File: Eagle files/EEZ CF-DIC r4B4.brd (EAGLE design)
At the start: 155 x 90 mm, 236 parts, among them IC1 VIPer35L, IC2 SI8233BB-D-IS1, IC3 LM5041B, IC4 LM258D, IC5 IR11688STRPBF, IC6 TL072, IC7 TL103W, P1 T910W-50K, Q1 MMBT5551, Q2 C3M0280090D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

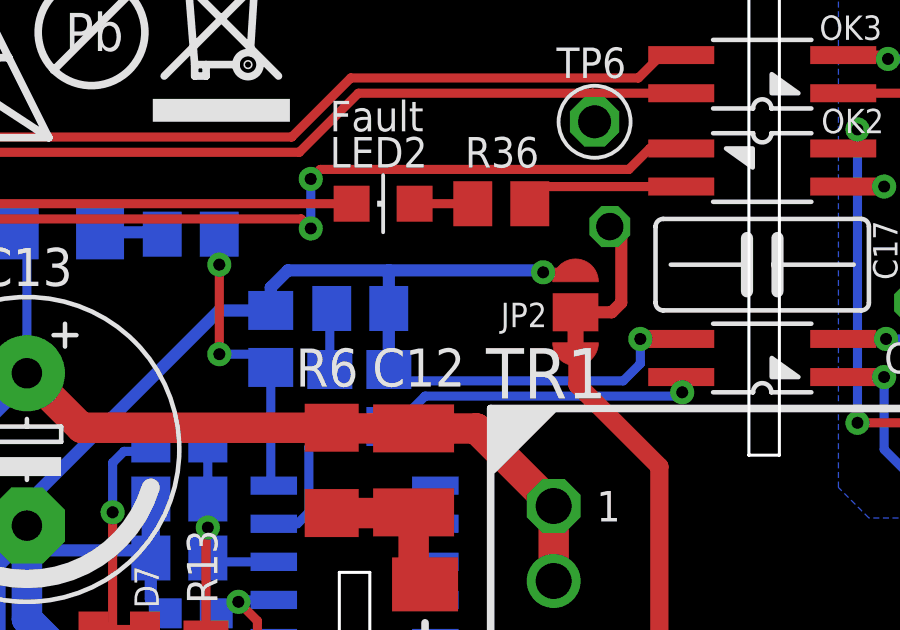
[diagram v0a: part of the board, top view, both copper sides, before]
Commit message: JP2 rotated
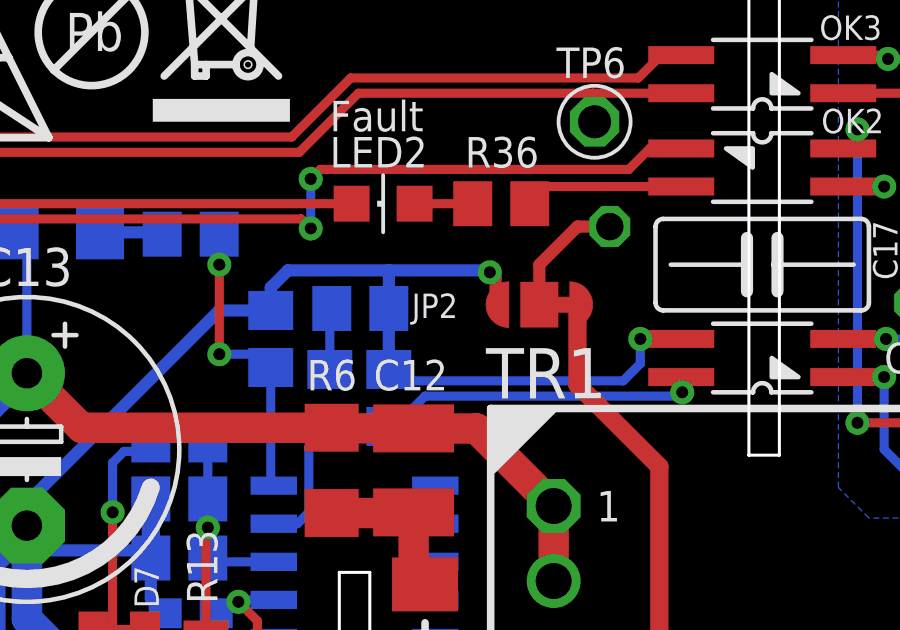
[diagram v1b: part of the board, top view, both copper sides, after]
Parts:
- moved JP2 1.23 mm to (99.0, 26.2), turned to 180 degrees
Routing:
- net 0V: track 763.4 -> 761.7 mm
- net PE: track 292.3 -> 293.8 mm
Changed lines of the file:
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@@
 <layer number="27" name="tValues" color="12" fill="1" visible="no" active="yes"/>
 <layer number="28" name="bValues" color="10" fill="1" visible="no" active="yes"/>
-<layer number="29" name="tStop" color="7" fill="1" visible="no" active="yes"/>
+<layer number="29" name="tStop" color="7" fill="1" visible="yes" active="yes"/>
 <layer number="30" name="bStop" color="7" fill="1" visible="no" active="yes"/>
 <layer number="31" name="tCream" color="7" fill="4" visible="no" active="yes"/>
@@
 <layer number="37" name="tTest" color="7" fill="1" visible="no" active="yes"/>
 <layer number="38" name="bTest" color="7" fill="1" visible="no" active="yes"/>
-<layer number="39" name="tKeepout" color="15" fill="1" visible="no" active="yes"/>
+<layer number="39" name="tKeepout" color="15" fill="1" visible="yes" active="yes"/>
 <layer number="40" name="bKeepout" color="5" fill="1" visible="no" active="yes"/>
 <layer number="41" name="tRestrict" color="14" fill="10" visible="no" active="yes"/>
@@
 </element>
 <element name="C12" library="rcl" package="C1210" value="1n/1kV" x="94.8055" y="20.6375" smashed="yes" rot="R270">
-<attribute name="NAME" x="96.52" y="24.7015" size="1.27" layer="25" ratio="10" rot="R180"/>
+<attribute name="NAME" x="93.472" y="23.3045" size="1.016" layer="25" ratio="10"/>
 <attribute name="VALUE" x="94.234" y="23.495" size="1.016" layer="27" ratio="10" rot="R270"/>
 </element>
@@
 </element>
 <element name="R6" library="rcl" package="R1206" value="220K" x="92.075" y="20.6375" smashed="yes" rot="R270">
-<attribute name="NAME" x="92.964" y="24.7015" size="1.27" layer="25" ratio="10" rot="R180"/>
+<attribute name="NAME" x="91.2495" y="23.3045" size="1.016" layer="25" ratio="10"/>
 <attribute name="VALUE" x="92.71" y="18.542" size="1.27" layer="27" rot="R90"/>
 </element>
@@
 <attribute name="NAME" x="145.7325" y="25.908" size="0.8128" layer="25" ratio="10"/>
 </element>
-<element name="JP2" library="EEZ_Lib1" package="JP3-CUT" value="JP3-CUT" x="100.203" y="25.908" smashed="yes" rot="R90">
-<attribute name="NAME" x="99.2505" y="26.2255" size="0.8128" layer="25" ratio="10" rot="R180"/>
+<element name="JP2" library="EEZ_Lib1" package="JP3-CUT" value="JP3-CUT" x="98.9965" y="26.162" smashed="yes" rot="R180">
+<attribute name="NAME" x="94.742" y="25.7175" size="0.8128" layer="25" ratio="10"/>
 </element>
 <element name="R61" library="rcl" package="R0805" value="47K" x="144.907" y="52.8955" smashed="yes" rot="MR270">
@@
 <wire x1="102.997" y1="1.4605" x2="102.997" y2="20.7645" width="0.6096" layer="1"/>
 <wire x1="102.997" y1="20.7645" x2="100.2665" y2="23.495" width="0.6096" layer="1"/>
-<wire x1="100.2665" y1="23.495" x2="100.2665" y2="24.5745" width="0.6096" layer="1"/>
-<wire x1="100.2665" y1="24.5745" x2="100.203" y2="24.638" width="0.6096" layer="1"/>
+<wire x1="100.2665" y1="23.495" x2="100.2665" y2="26.162" width="0.6096" layer="1"/>
 <contactref element="X3" pad="8"/>
 <wire x1="145.9865" y1="1.4605" x2="147.32" y2="2.794" width="0.6096" layer="1"/>
@@
 <wire x1="102.362" y1="25.019" x2="102.362" y2="24.1935" width="0.3048" layer="16"/>
 <wire x1="102.362" y1="24.1935" x2="101.7905" y2="23.622" width="0.3048" layer="16"/>
-<via x="99.1235" y="27.2415" extent="1-16" drill="0.4" shape="octagon"/>
+<via x="97.3455" y="27.2415" extent="1-16" drill="0.4" shape="octagon"/>
 <wire x1="101.7905" y1="23.622" x2="94.3585" y2="23.622" width="0.3048" layer="16"/>
 <wire x1="94.3585" y1="23.622" x2="93.98" y2="24.0005" width="0.3048" layer="16"/>
@@
 <wire x1="56.7182" y1="23.468990625" x2="57.874509375" y2="23.468990625" width="0.3048" layer="1"/>
 <wire x1="57.874509375" y1="23.468990625" x2="57.9755" y2="23.368" width="0.3048" layer="1"/>
-<wire x1="99.06" y1="27.305" x2="99.1235" y2="27.2415" width="0.4064" layer="16"/>
 <wire x1="90.043" y1="25.969" x2="90.043" y2="26.7335" width="0.4064" layer="16"/>
 <wire x1="90.043" y1="26.7335" x2="90.6145" y2="27.305" width="0.4064" layer="16"/>
-<wire x1="99.1235" y1="27.2415" x2="100.076" y2="27.2415" width="0.3048" layer="1"/>
-<wire x1="100.076" y1="27.2415" x2="100.203" y2="27.3685" width="0.3048" layer="1"/>
-<wire x1="99.06" y1="27.305" x2="93.98" y2="27.305" width="0.4064" layer="16"/>
+<wire x1="97.282" y1="27.305" x2="93.98" y2="27.305" width="0.4064" layer="16"/>
 <wire x1="93.98" y1="27.305" x2="93.98" y2="26.0375" width="0.4064" layer="16"/>
 <wire x1="93.98" y1="26.0375" x2="93.9775" y2="26.035" width="0.4064" layer="16"/>
@@
 <wire x1="98.6142" y1="7.8105" x2="89.408" y2="7.8105" width="0.6096" layer="16"/>
 <wire x1="89.408" y1="7.8105" x2="86.233" y2="10.9855" width="0.6096" layer="16"/>
+<wire x1="97.536" y1="26.162" x2="97.536" y2="27.051" width="0.4064" layer="1"/>
+<wire x1="97.536" y1="27.051" x2="97.3455" y2="27.2415" width="0.4064" layer="1"/>
+<wire x1="97.282" y1="27.305" x2="97.3455" y2="27.2415" width="0.4064" layer="16"/>
 <wire x1="19.558" y1="6.156" x2="19.6755" y2="6.1595" width="0" layer="19" extent="1-1"/>
 </signal>
@@
 <contactref element="C17" pad="1"/>
 <contactref element="JP2" pad="COM"/>
-<wire x1="100.203" y1="25.908" x2="101.4095" y2="25.908" width="0.4064" layer="1"/>
-<wire x1="101.4095" y1="25.908" x2="101.727" y2="26.2255" width="0.4064" layer="1"/>
-<wire x1="101.727" y1="26.2255" x2="101.727" y2="28.3845" width="0.4064" layer="1"/>
-<wire x1="101.727" y1="28.3845" x2="101.346" y2="28.7655" width="0.4064" layer="1"/>
+<wire x1="98.9965" y1="26.162" x2="98.9965" y2="27.4955" width="0.4064" layer="1"/>
+<wire x1="98.9965" y1="27.4955" x2="100.2665" y2="28.7655" width="0.4064" layer="1"/>
+<wire x1="100.2665" y1="28.7655" x2="101.346" y2="28.7655" width="0.4064" layer="1"/>
 </signal>
 <signal name="N$18">

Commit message: PWRGOOD renamed to FAULT
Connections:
- net PWRGOOD renamed !FAULT
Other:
- board text added: "4 !FAULT!"
- board text added: "5 V+"
- board text added: "7 V-"
- board text removed: "4 Pwrgood"
- board text removed: "5 +5Vdc"
- board text removed: "7 -5Vdc"

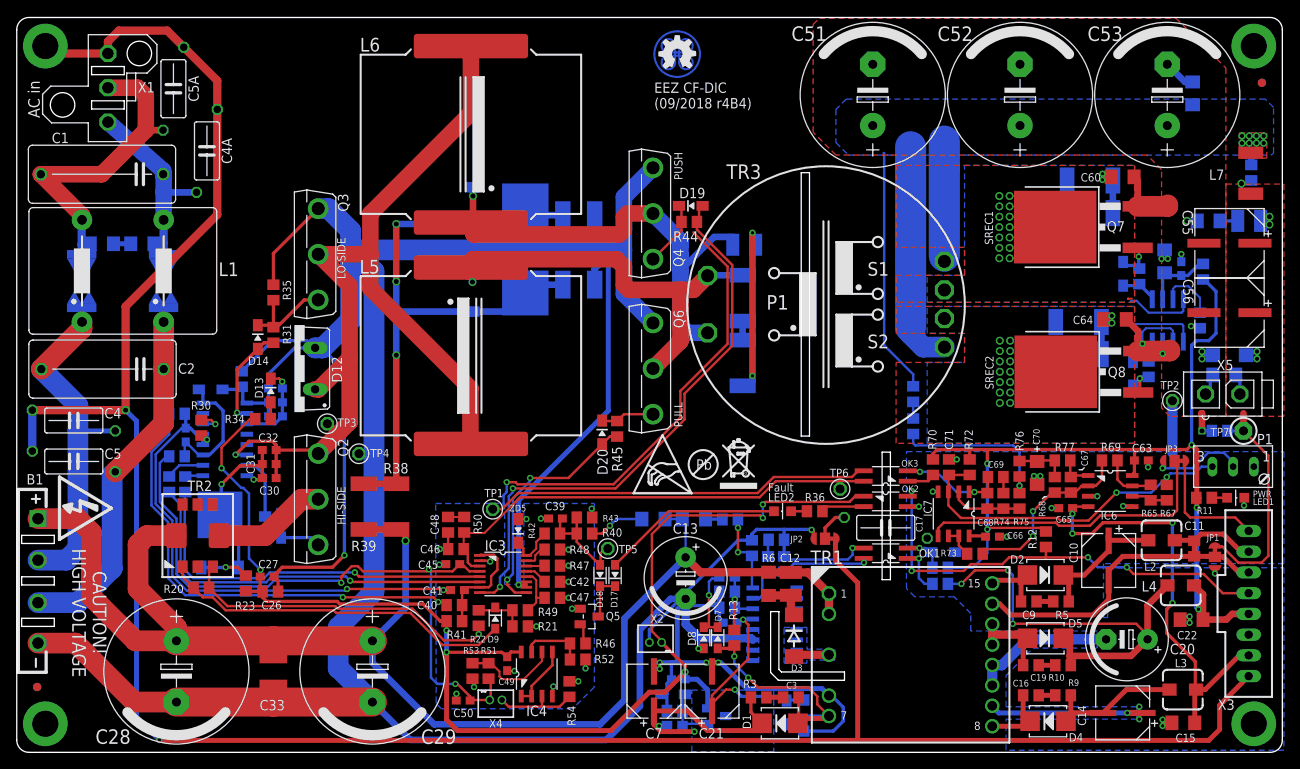
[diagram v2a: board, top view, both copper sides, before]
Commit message: #1, power inductors rotated, shorter PUSH gate trace
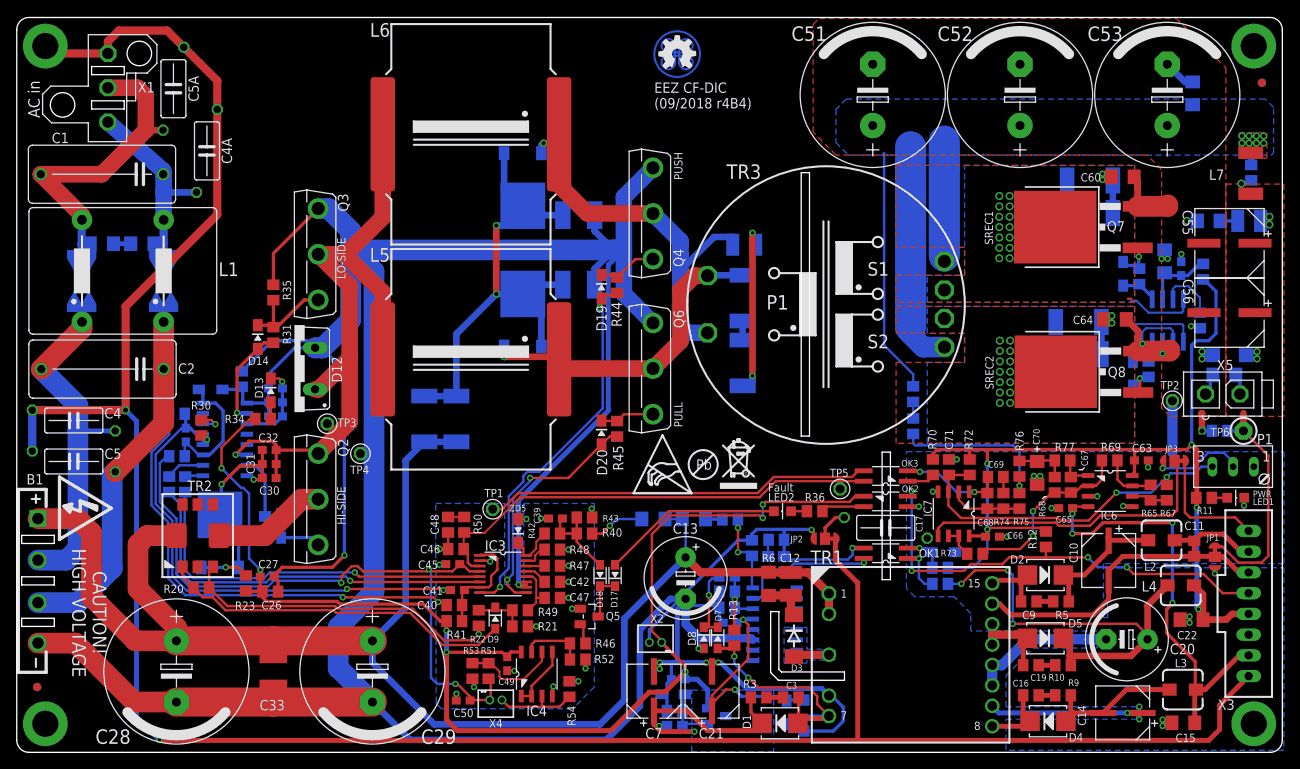
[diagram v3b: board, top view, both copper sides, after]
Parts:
- removed TP7: (no value), EEZ_Lib1:TP_1.1MM_2
- TP6: device EEZ_Lib1:PCB_SHIELD_TAB -> EEZ_Lib1:TP_1.1MM_2
- moved TP6 49.9 mm to (150.2, 39.4), turned to 180 degrees
- moved TP5 29.4 mm to (100.8, 32.3), turned to 90 degrees
- moved D19 14.7 mm to (71.6, 57.0), turned to 270 degrees
- moved R39 13.1 mm to (49.9, 40.8), flipped to the bottom
- moved R38 13.0 mm to (53.8, 40.8), flipped to the bottom
- moved R44 11.7 mm to (73.5, 57.2), turned to 270 degrees
- moved D15 1.25 mm to (62.0, 55.2), turned to 0 degrees
- moved D16 1.14 mm to (62.0, 67.9), turned to 180 degrees
- moved L5 0.44 mm to (55.6, 48.1), turned to 180 degrees
- moved TP4 0.19 mm to (42.1, 36.6)
- moved D20 0.06 mm to (71.6, 39.2)
- turned L6 to 180 degrees
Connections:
- net GND: now also TP6.GND; no longer TP7.GND
- net ISO_FB: now also TP5.1; no longer TP6.1
- net PREG_OUT+: now also TP6.TIP; no longer TP7.TIP
- net ULVO: no longer TP5.1
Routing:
- net 0V: track 761.7 -> 707.0 mm, vias 34 -> 33
- net BUCK_OUT: track 118.7 -> 86.8 mm
- net PUSH: track 70.9 -> 46.8 mm
- net CLAMP_C: track 79.4 -> 59.9 mm, vias 3 -> 2
- net L_PULL: track 51.5 -> 40.0 mm
- net DC_BUS: track 180.8 -> 190.7 mm, vias 1 -> 0
- net L_PUSH: track 60.4 -> 50.7 mm
- net ULVO: track 13.6 -> 11.1 mm
- net N$13: track 8.09 -> 7.35 mm
